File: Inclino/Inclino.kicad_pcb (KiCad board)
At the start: 2 copper layers, 171.4 x 91.4 mm, 44 parts, among them P1 Prog, Q1 PMV65UN, SW1 SW_Push, SW2 SW_Push, SW3 SW_Push, SW4 SW_Push, U1 MAX7219, U10 TPS61032PWP, U2 SCA103T-D04, U3 7SEGMENT_CC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

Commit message: Send Inclino PCB
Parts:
- removed R8: 100k, Yame_library:SM0603-MR
- added CutHole_1: VAL**, Yame_library:CutHole_1, F.Cu at (110.0, 129.0)
- added CutHole_1: VAL**, Yame_library:CutHole_1, F.Cu at (122.0, 129.0)
- added CutHole_1: VAL**, Yame_library:CutHole_1, F.Cu at (107.0, 129.0)
- added CutHole_1: VAL**, Yame_library:CutHole_1, F.Cu at (108.5, 129.0)
- added CutHole_1: VAL**, Yame_library:CutHole_1, F.Cu at (105.5, 129.0)
- added CutHole_1: VAL**, Yame_library:CutHole_1, F.Cu at (95.0, 129.0)
- added CutHole_1: VAL**, Yame_library:CutHole_1, F.Cu at (98.0, 129.0)
- added CutHole_1: VAL**, Yame_library:CutHole_1, F.Cu at (96.5, 129.0)
- added CutHole_1: VAL**, Yame_library:CutHole_1, F.Cu at (102.5, 129.0)
- added CutHole_1: VAL**, Yame_library:CutHole_1, F.Cu at (104.0, 129.0)
- added CutHole_1: VAL**, Yame_library:CutHole_1, F.Cu at (101.0, 129.0)
- added CutHole_1: VAL**, Yame_library:CutHole_1, F.Cu at (111.5, 129.0)
- added CutHole_1: VAL**, Yame_library:CutHole_1, F.Cu at (99.5, 129.0)
- added CutHole_1: VAL**, Yame_library:CutHole_1, F.Cu at (114.5, 129.0)
- added CutHole_1: VAL**, Yame_library:CutHole_1, F.Cu at (113.0, 129.0)
- added CutHole_1: VAL**, Yame_library:CutHole_1, F.Cu at (119.0, 129.0)
- added CutHole_1: VAL**, Yame_library:CutHole_1, F.Cu at (120.5, 129.0)
- added CutHole_1: VAL**, Yame_library:CutHole_1, F.Cu at (117.5, 129.0)
- added CutHole_1: VAL**, Yame_library:CutHole_1, F.Cu at (116.0, 129.0)
- added CutHole_1: VAL**, Yame_library:CutHole_1, F.Cu at (123.5, 129.0)
- added J1: Fix, Mounting_Holes:MountingHole_3.2mm_M3, F.Cu at (28.5, 176.5)
- added J2: Fix, Mounting_Holes:MountingHole_3.2mm_M3, F.Cu at (121.5, 133.5)
- added J3: Conn_01x03, Yame_library:Inc_90°, F.Cu at (64.2, 159.5)
- added J4: Conn_01x03, Yame_library:Inc_90°, F.Cu at (64.2, 165.7)
- added J5: Conn_01x03, Yame_library:Inc_90°, F.Cu at (97.2, 123.6)
- added J6: Conn_01x03, Yame_library:Inc_90°, B.Cu at (97.2, 123.6)
- C10, C11, C12, C13, C3, C4, C8, C9, L1, Q1, R1, R10, R11, R12, R9, U1, U10, U7: moved to B.Cu
- SW4: value SW_Push -> SW_Power
- moved U1 169.1 mm to (40.7, 159.2), turned to 270 degrees
- moved C6 162.1 mm to (47.7, 174.8), turned to 270 degrees
- moved C5 154.7 mm to (57.7, 174.8), turned to 270 degrees
- moved R6 154.5 mm to (47.7, 171.9), turned to 90 degrees
- moved U9 153.8 mm to (33.5, 142.0)
- moved R2 152.7 mm to (47.7, 169.0), turned to 90 degrees
- moved C7 152.0 mm to (37.7, 174.8), turned to 270 degrees
- moved SW1 151.5 mm to (45.0, 173.5), turned to 90 degrees
- moved C3 149.7 mm to (39.4, 166.0), turned to 180 degrees
- moved R5 148.4 mm to (57.7, 171.9), turned to 90 degrees
- moved R4 148.0 mm to (57.7, 169.0), turned to 90 degrees
- moved R7 147.5 mm to (37.7, 171.9), turned to 90 degrees
- moved R3 145.6 mm to (37.7, 169.0), turned to 90 degrees
- moved SW3 145.0 mm to (55.0, 173.5), turned to 90 degrees
- moved R1 142.3 mm to (41.8, 166.8), turned to 90 degrees
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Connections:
- net Net-(L1-Pad2) renamed /+Vsw
- BT2 pad 2: Net-(BT2-Pad2) -> /BATT_LowSide
- C1 pad 1: /+5v -> /+5v_R
- C1 pad 2: GND -> /GND_R
- C2 pad 1: /+5v -> /+5v_R
- C2 pad 2: GND -> /GND_R
- Q1 pad 2: Net-(BT2-Pad2) -> GND
- Q1 pad 3: GND -> /BATT_LowSide
- R12 pad 1: Net-(BT2-Pad2) -> /Von
- R12 pad 2: /Von -> GND
- SW4 pad 1: /+Vbat -> /BATT_LowSide
- SW4 pad 2: /Von -> GND
- U2 pad 1: /SCK -> /SCK_R
- U2 pad 12: /+5v -> /+5v_R
- U2 pad 3: /MISO -> /MISO_R
- U2 pad 4: /MOSI -> /MOSI_R
- U2 pad 6: GND -> /GND_R
- U2 pad 7: //CS_INC -> //CS_INC_R
- U7 pad 10: Net-(R8-Pad2) -> /Von
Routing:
- net GND: track 0.00 -> 412.6 mm, vias 0 -> 42
- net /DP: track 0.00 -> 143.7 mm, vias 0 -> 6
- net /A: track 0.00 -> 140.1 mm, vias 0 -> 5
- net /B: track 0.00 -> 139.6 mm, vias 0 -> 6
- net /+5v: track 0.00 -> 138.7 mm, vias 0 -> 3
- net /F: track 0.00 -> 131.7 mm, vias 0 -> 5
- net /C: track 0.00 -> 126.4 mm, vias 0 -> 6
- net /D: track 0.00 -> 126.2 mm, vias 0 -> 6
- net /G: track 0.00 -> 125.8 mm, vias 0 -> 5
- net /E: track 0.00 -> 113.6 mm, vias 0 -> 6
- net /D0: track 0.00 -> 94.9 mm, vias 0 -> 1
- net /MOSI: track 0.00 -> 76.4 mm, vias 0 -> 5
- net /SCK: track 0.00 -> 69.3 mm, vias 0 -> 3
- net /D1: track 0.00 -> 65.9 mm, vias 0 -> 1
- net /D2: track 0.00 -> 58.7 mm, vias 0 -> 1
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- added copper zone on B.Cu, net /+5v
- added copper zone on B.Cu, net /+Vbat
- added copper zone on B.Cu, net /+Vsw
- added copper zone on B.Cu, net /GND_R
- added copper zone on F.Cu, net /GND_R
- added copper zone on B.Cu, net GND
- added copper zone on F.Cu, net GND
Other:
- board size 171.4 x 91.4 mm -> 100 x 73.5 mm

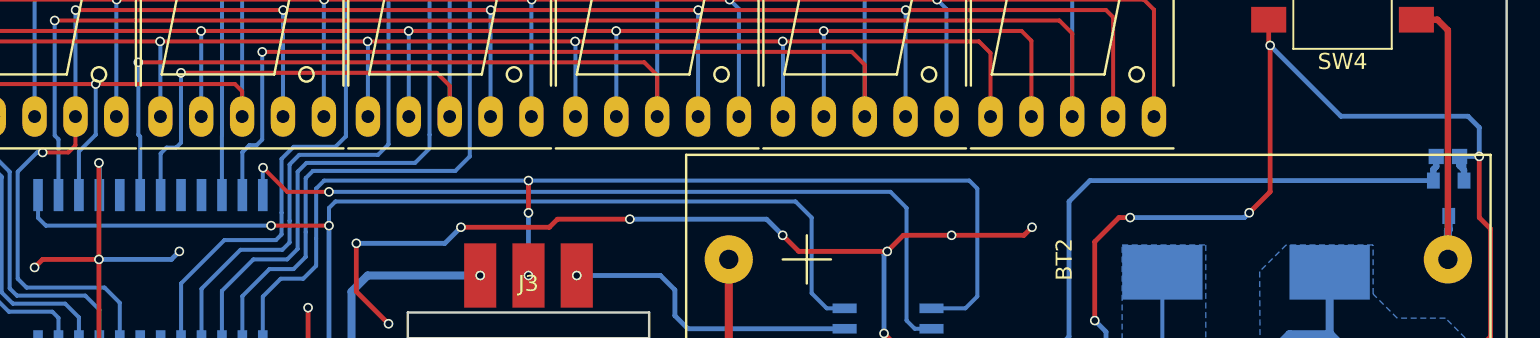
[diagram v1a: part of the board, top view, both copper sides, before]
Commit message: Fix Inclino bug
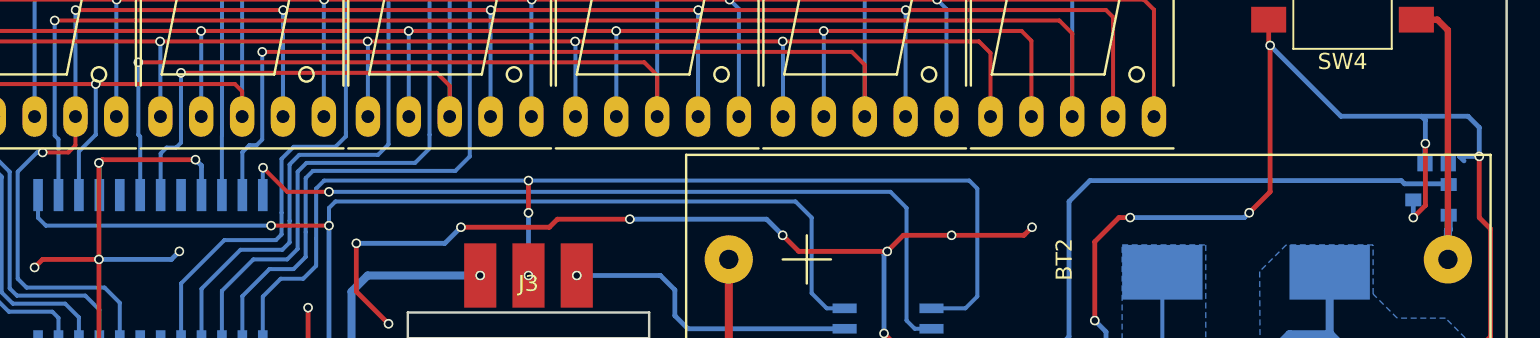
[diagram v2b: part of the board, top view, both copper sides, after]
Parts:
- moved Q1 1.10 mm to (120.3, 154.8), turned to 270 degrees
- moved R12 0.83 mm to (120.7, 152.6), turned to 180 degrees
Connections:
- Q1 pad 2: GND -> /BATT_LowSide
- Q1 pad 3: /BATT_LowSide -> GND
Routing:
- net GND: track 412.6 -> 427.2 mm, vias 42 -> 45
- net /Von: track 42.0 -> 42.8 mm
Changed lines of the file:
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@@
   (general
     (links 159)
-    (no_connects 1)
-    (area 24.924999 129.924999 125.075001 180.075001)
+    (no_connects 0)
+    (area 24.924999 106.424999 125.075001 180.075001)
     (thickness 1.6)
     (drawings 15)
-    (tracks 848)
+    (tracks 862)
     (zones 0)
     (modules 69)
@@
   )
   (module Yame_library:SOT23-MR placed (layer B.Cu)
-    (at 121.4 154.7)
+    (at 120.3 154.8 270)
     (tags SOT23)
     (attr smd)
-    (fp_text reference Q1 (at 0.2 -0.1 180) (layer B.SilkS)
+    (fp_text reference Q1 (at 0.2 -0.1 450) (layer B.SilkS)
       (effects (font (size 0.5 0.5) (thickness 0.11938)) (justify mirror))
     )
-    (fp_text value PMV65UN (at 0.0635 0) (layer B.SilkS) hide
+    (fp_text value PMV65UN (at 0.0635 0 270) (layer B.SilkS) hide
       (effects (font (size 0.50038 0.50038) (thickness 0.09906)) (justify mirror))
     )
@@
     (fp_line (start 1.27 -0.508) (end -1.3335 -0.508) (layer B.SilkS) (width 0.07874))
     (fp_line (start -1.3335 0.508) (end 1.27 0.508) (layer B.SilkS) (width 0.07874))
-    (pad 3 smd rect (at 0 1.09982) (size 0.8001 1.00076) (layers B.Cu B.Paste B.Mask)
+    (pad 3 smd rect (at 0 1.09982 270) (size 0.8001 1.00076) (layers B.Cu B.Paste B.Mask)
+      (net 4 GND))
+    (pad 2 smd rect (at 0.9525 -1.09982 270) (size 0.8001 1.00076) (layers B.Cu B.Paste B.Mask)
       (net 51 /BATT_LowSide))
-    (pad 2 smd rect (at 0.9525 -1.09982) (size 0.8001 1.00076) (layers B.Cu B.Paste B.Mask)
-      (net 4 GND))
-    (pad 1 smd rect (at -0.9525 -1.09982) (size 0.8001 1.00076) (layers B.Cu B.Paste B.Mask)
+    (pad 1 smd rect (at -0.9525 -1.09982 270) (size 0.8001 1.00076) (layers B.Cu B.Paste B.Mask)
       (net 11 /Von))
     (model smd\SOT23_3.wrl
@@
   )
   (module Yame_library:SM0603-MR placed (layer B.Cu)
-    (at 121.35 152.1)
-    (attr smd)
-    (fp_text reference R12 (at 0 0) (layer B.SilkS)
+    (at 120.65 152.55 180)
+    (attr smd)
+    (fp_text reference R12 (at 0 0 180) (layer B.SilkS)
       (effects (font (size 0.508 0.4572) (thickness 0.1143)) (justify mirror))
     )
-    (fp_text value 1M (at 0 0) (layer B.SilkS) hide
+    (fp_text value 1M (at 0 0 180) (layer B.SilkS) hide
       (effects (font (size 0.508 0.4572) (thickness 0.1143)) (justify mirror))
     )
@@
     (fp_line (start -1.3 -0.6) (end 1.3 -0.6) (layer B.SilkS) (width 0.15))
     (fp_line (start 1.3 -0.6) (end 1.3 0.6) (layer B.SilkS) (width 0.15))
-    (pad 1 smd rect (at -0.725 0) (size 0.95 0.95) (layers B.Cu B.Paste B.Mask)
+    (pad 1 smd rect (at -0.725 0 180) (size 0.95 0.95) (layers B.Cu B.Paste B.Mask)
       (net 11 /Von))
-    (pad 2 smd rect (at 0.725 0) (size 0.95 0.95) (layers B.Cu B.Paste B.Mask)
+    (pad 2 smd rect (at 0.725 0 180) (size 0.95 0.95) (layers B.Cu B.Paste B.Mask)
       (net 4 GND))
     (model smd\resistors\R0603.wrl
@@
   (segment (start 40.065 165.94) (end 40.075 165.95) (width 0.4) (layer B.Cu) (net 3))
   (segment (start 40.075 165.95) (end 40.075 167.6) (width 0.4) (layer B.Cu) (net 3))
+  (segment (start 43.875 154.5) (end 43.875 152.675) (width 0.3) (layer B.Cu) (net 4) (status 400000))
+  (segment (start 37.7 152.3) (end 37.5 152.5) (width 0.3) (layer F.Cu) (net 4))
+  (segment (start 43.5 152.3) (end 37.7 152.3) (width 0.3) (layer F.Cu) (net 4))
+  (via (at 43.5 152.3) (size 0.6) (drill 0.4) (layers F.Cu B.Cu) (net 4))
+  (segment (start 43.875 152.675) (end 43.5 152.3) (width 0.3) (layer B.Cu) (net 4))
+  (segment (start 119.95 151.3) (end 119.95 149.85) (width 0.3) (layer B.Cu) (net 4))
+  (segment (start 119.95 149.85) (end 119.7 149.6) (width 0.3) (layer B.Cu) (net 4))
+  (segment (start 119.20018 154.8) (end 119.20018 155.89982) (width 0.3) (layer B.Cu) (net 4) (status 400000))
+  (segment (start 119.925 151.325) (end 119.925 152.55) (width 0.3) (layer B.Cu) (net 4) (status 800000))
+  (segment (start 119.95 151.3) (end 119.925 151.325) (width 0.3) (layer B.Cu) (net 4))
+  (via (at 119.95 151.3) (size 0.6) (drill 0.4) (layers F.Cu B.Cu) (net 4))
+  (segment (start 119.95 155.15) (end 119.95 151.3) (width 0.3) (layer F.Cu) (net 4))
+  (segment (start 119.2 155.9) (end 119.95 155.15) (width 0.3) (layer F.Cu) (net 4))
+  (via (at 119.2 155.9) (size 0.6) (drill 0.4) (layers F.Cu B.Cu) (net 4))
+  (segment (start 119.20018 155.89982) (end 119.2 155.9) (width 0.3) (layer B.Cu) (net 4))
   (segment (start 53.5 157.5) (end 53.5 160.5) (width 0.3) (layer F.Cu) (net 4))
   (segment (start 66 156) (end 65.5 156.5) (width 0.3) (layer F.Cu) (net 4))
@@
   (segment (start 109.375 169.025) (end 108.85 168.5) (width 0.3) (layer B.Cu) (net 4))
   (segment (start 122.075 152.1) (end 123.3 152.1) (width 0.3) (layer B.Cu) (net 4))
-  (segment (start 122.3525 153.60018) (end 122.3525 152.3775) (width 0.3) (layer B.Cu) (net 4))
   (segment (start 122.3525 152.3775) (end 122.075 152.1) (width 0.3) (layer B.Cu) (net 4))
   (segment (start 57.7 166.8) (end 57.7 169.3) (width 0.3) (layer B.Cu) (net 4))
@@
   (segment (start 110.21 143.6) (end 110.21 145.11) (width 0.3) (layer F.Cu) (net 4))
   (segment (start 123.3 150.3) (end 123.3 152.1) (width 0.3) (layer B.Cu) (net 4))
+  (segment (start 122.6 149.6) (end 123.3 150.3) (width 0.3) (layer B.Cu) (net 4))
+  (segment (start 119.7 149.6) (end 122.6 149.6) (width 0.3) (layer B.Cu) (net 4))
   (via (at 110.3 145.2) (size 0.6) (drill 0.4) (layers F.Cu B.Cu) (net 4))
+  (segment (start 114.7 149.6) (end 119.7 149.6) (width 0.3) (layer B.Cu) (net 4))
   (segment (start 110.3 145.2) (end 114.7 149.6) (width 0.3) (layer B.Cu) (net 4))
-  (segment (start 114.7 149.6) (end 122.6 149.6) (width 0.3) (layer B.Cu) (net 4))
-  (segment (start 122.6 149.6) (end 123.3 150.3) (width 0.3) (layer B.Cu) (net 4))
   (segment (start 110.21 145.11) (end 110.3 145.2) (width 0.3) (layer F.Cu) (net 4))
   (segment (start 79.75 175.375) (end 79.75 176.2) (width 0.5) (layer B.Cu) (net 4))
@@
   (segment (start 110.675 175.275) (end 110.675 173.475) (width 0.4) (layer B.Cu) (net 4))
   (segment (start 110.675 173.475) (end 109.7 172.5) (width 0.4) (layer B.Cu) (net 4))
-  (segment (start 122.075 152.1) (end 122.075 152.675) (width 0.4) (layer B.Cu) (net 4))
-  (segment (start 122.3525 152.9525) (end 122.3525 153.60018) (width 0.4) (layer B.Cu) (net 4))
-  (segment (start 122.075 152.675) (end 122.3525 152.9525) (width 0.4) (layer B.Cu) (net 4))
   (segment (start 89.25 165.35) (end 86.85 165.35) (width 0.3) (layer B.Cu) (net 5))
   (segment (start 58.775 174.075) (end 57.7 174.075) (width 0.25) (layer F.Cu) (net 5))
@@
   (segment (start 85.9 165.7) (end 85.9 172.1) (width 0.3) (layer B.Cu) (net 10))
   (segment (start 85.55 165.35) (end 85.9 165.7) (width 0.3) (layer B.Cu) (net 10))
+  (segment (start 121.39982 153.8475) (end 121.375 153.82268) (width 0.3) (layer B.Cu) (net 11) (status C00000))
+  (segment (start 121.375 153.82268) (end 121.375 152.55) (width 0.3) (layer B.Cu) (net 11) (status C00000))
+  (segment (start 99.09982 153.60018) (end 118.45018 153.60018) (width 0.3) (layer B.Cu) (net 11))
+  (segment (start 97.02 164.08) (end 97.8 163.3) (width 0.3) (layer B.Cu) (net 11))
+  (segment (start 97.8 163.3) (end 97.8 154.9) (width 0.3) (layer B.Cu) (net 11))
+  (segment (start 97.8 154.9) (end 99.09982 153.60018) (width 0.3) (layer B.Cu) (net 11))
   (segment (start 89.25 164.08) (end 97.02 164.08) (width 0.3) (layer B.Cu) (net 11))
-  (segment (start 99.09982 153.60018) (end 120.4475 153.60018) (width 0.3) (layer B.Cu) (net 11))
-  (segment (start 97.8 154.9) (end 99.09982 153.60018) (width 0.3) (layer B.Cu) (net 11))
-  (segment (start 97.8 163.3) (end 97.8 154.9) (width 0.3) (layer B.Cu) (net 11))
-  (segment (start 97.02 164.08) (end 97.8 163.3) (width 0.3) (layer B.Cu) (net 11))
-  (segment (start 120.4475 153.60018) (end 120.4475 152.9025) (width 0.4) (layer B.Cu) (net 11))
-  (segment (start 120.625 152.725) (end 120.625 152.1) (width 0.4) (layer B.Cu) (net 11))
-  (segment (start 120.4475 152.9025) (end 120.625 152.725) (width 0.4) (layer B.Cu) (net 11))
+  (segment (start 118.65 153.8) (end 121.35232 153.8) (width 0.3) (layer B.Cu) (net 11) (status 800000))
+  (segment (start 118.45018 153.60018) (end 118.65 153.8) (width 0.3) (layer B.Cu) (net 11))
+  (segment (start 121.35232 153.8) (end 121.39982 153.8475) (width 0.3) (layer B.Cu) (net 11) (status C00000))
   (segment (start 47.7 169.725) (end 47.7 171.175) (width 0.3) (layer F.Cu) (net 12))
   (segment (start 45 168.91) (end 46.01 168.91) (width 0.3) (layer F.Cu) (net 12))
@@
   (segment (start 72.4 159.5) (end 73.3 160.4) (width 0.3) (layer B.Cu) (net 41))
   (segment (start 72.4 159.5) (end 67.2 159.5) (width 0.3) (layer B.Cu) (net 41))
+  (segment (start 121.4 156.65) (end 121.4 155.79982) (width 0.5) (layer B.Cu) (net 51))
   (segment (start 119.39 143.6) (end 120.7 143.6) (width 0.4) (layer F.Cu) (net 51))
   (segment (start 121.35 144.25) (end 121.35 158.5) (width 0.4) (layer F.Cu) (net 51))
   (segment (start 120.7 143.6) (end 121.35 144.25) (width 0.4) (layer F.Cu) (net 51))
   (segment (start 121.35 158.5) (end 121.35 156.7) (width 0.5) (layer B.Cu) (net 51))
-  (segment (start 121.4 156.65) (end 121.4 155.79982) (width 0.5) (layer B.Cu) (net 51))
   (segment (start 121.35 156.7) (end 121.4 156.65) (width 0.5) (layer B.Cu) (net 51))
   (segment (start 107.425 169.725) (end 107.425 168.725) (width 0.25) (layer B.Cu) (net 52))
